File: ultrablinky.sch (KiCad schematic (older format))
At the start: 124 parts, among them J1 DNP, J2 SJ1-3523N, J3 SJ1-3523N, J4 Barrel_Jack_5.5x2.5, J5 DNP, J6 DNP, J7 Terminal5, J8 SJ1-3523N, Q1 DMP6180SK3Q-13, Q2 DMP6180SK3Q-13, Q4 MMBT3906, Q5 MMBT3904, Q6 MMBT3904, Q7 IRFZ44ZPBF, Q8 MMBT3904, SW1 SW_SPDT, SW2 PEC11R-4215F-S0024, SW3 SW_Push, U1 SGTL5000, U10 74VHC1G09, U2 TPS73618DBV, U3 Teensy4.0, U4 4N25, U5 LM2574HVM-5, U6 MC34071ADR2G, U7 DNP, U8 MCP4706A1T-E/CH, U9 VXO7803-500

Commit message: Changed film caps to electrolytic
The film caps in the audio path were changed to electrolytic in order to
bring down the cost and have better availability
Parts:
- C15, C23, C28: Source Mouser 80-C0805C101J1G -> Mouser 80-C0805C101J1G
- C2, C3, C5, C6: footprint 0_my_footprints:RSBCC4220Z310K_film_cap -> Capacitor_SMD:CP_Elec_4x5.7; symbol Device:C -> Device:CP; Source Mouser 80-RSBCC4220Z310K -> Mouser 710-865080140002
- C4: footprint 0_my_footprints:RSBCC4220Z310K_film_cap -> Capacitor_SMD:CP_Elec_4x5.7; symbol Device:C -> Device:CP; Source Mouser 80-RSBCC4220Z310K -> (none)
- R1: Source Mouser 603-RC0805JR-132K2L -> (none)
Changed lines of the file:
@@
 F 2 "Capacitor_SMD:C_0805_2012Metric" H 1738 8450 50  0001 C CNN
 F 3 "~" H 1700 8600 50  0001 C CNN
-F 4 "Mouser 80-C0805C101J1G " H 1700 8600 50  0001 C CNN "Source"
+F 4 "Mouser 80-C0805C101J1G" H 1700 8600 50  0001 C CNN "Source"
 	1    1700 8600
 	1    0    0    -1
@@
 F 2 "Capacitor_SMD:C_0805_2012Metric" H 13838 2000 50  0001 C CNN
 F 3 "~" H 13800 2150 50  0001 C CNN
-F 4 "Mouser 80-C0805C101J1G " H 13800 2150 50  0001 C CNN "Source"
+F 4 "Mouser 80-C0805C101J1G" H 13800 2150 50  0001 C CNN "Source"
 	1    13800 2150
 	1    0    0    -1
@@
 F 2 "Resistor_SMD:R_0805_2012Metric" V 11530 6650 50  0001 C CNN
 F 3 "~" H 11600 6650 50  0001 C CNN
-F 4 "Mouser 603-RC0805JR-132K2L" H 11600 6650 50  0001 C CNN "Source"
+F 4 "~" H 11600 6650 50  0001 C CNN "Source"
 	1    11600 6650
 	0    -1   1    0
@@
 $EndComp
 $Comp
-L Device:C C3
+L Device:CP C3
 U 1 1 61893B69
 P 11900 6050
-F 0 "C3" V 11850 6200 50  0000 C CNN
+F 0 "C3" V 11850 6250 50  0000 C CNN
 F 1 "2.2uF" V 11850 5900 50  0000 C CNN
-F 2 "0_my_footprints:RSBCC4220Z310K_film_cap" H 11938 5900 50  0001 C CNN
+F 2 "Capacitor_SMD:CP_Elec_4x5.7" H 11938 5900 50  0001 C CNN
 F 3 "~" H 11900 6050 50  0001 C CNN
-F 4 "Mouser 80-RSBCC4220Z310K" H 11900 6050 50  0001 C CNN "Source"
+F 4 "Mouser 710-865080140002" H 11900 6050 50  0001 C CNN "Source"
 	1    11900 6050
 	0    1    1    0
 $EndComp
 $Comp
-L Device:C C2
+L Device:CP C2
 U 1 1 61899EFD
 P 11900 6250
-F 0 "C2" V 11850 6400 50  0000 C CNN
+F 0 "C2" V 11850 6450 50  0000 C CNN
 F 1 "2.2uF" V 11850 6100 50  0000 C CNN
-F 2 "0_my_footprints:RSBCC4220Z310K_film_cap" H 11938 6100 50  0001 C CNN
+F 2 "Capacitor_SMD:CP_Elec_4x5.7" H 11938 6100 50  0001 C CNN
 F 3 "~" H 11900 6250 50  0001 C CNN
-F 4 "Mouser 80-RSBCC4220Z310K" H 11900 6250 50  0001 C CNN "Source"
+F 4 "Mouser 710-865080140002" H 11900 6250 50  0001 C CNN "Source"
 	1    11900 6250
 	0    1    1    0
 $EndComp
 $Comp
-L Device:C C4
+L Device:CP C4
 U 1 1 6189A492
 P 11900 6500
-F 0 "C4" V 11850 6650 50  0000 C CNN
+F 0 "C4" V 11850 6700 50  0000 C CNN
 F 1 "DNP" V 11850 6350 50  0000 C CNN
-F 2 "0_my_footprints:RSBCC4220Z310K_film_cap" H 11938 6350 50  0001 C CNN
+F 2 "Capacitor_SMD:CP_Elec_4x5.7" H 11938 6350 50  0001 C CNN
 F 3 "~" H 11900 6500 50  0001 C CNN
-F 4 "Mouser 80-RSBCC4220Z310K" H 11900 6500 50  0001 C CNN "Source"
+F 4 "~" H 11900 6500 50  0001 C CNN "Source"
 	1    11900 6500
 	0    1    1    0
 $EndComp
 $Comp
-L Device:C C6
+L Device:CP C6
 U 1 1 6189AB69
 P 14700 6400
-F 0 "C6" V 14450 6400 50  0000 C CNN
-F 1 "2.2uF" V 14550 6400 50  0000 C CNN
-F 2 "0_my_footprints:RSBCC4220Z310K_film_cap" H 14738 6250 50  0001 C CNN
+F 0 "C6" V 14950 6400 50  0000 C CNN
+F 1 "2.2uF" V 14850 6400 50  0000 C CNN
+F 2 "Capacitor_SMD:CP_Elec_4x5.7" H 14738 6250 50  0001 C CNN
 F 3 "~" H 14700 6400 50  0001 C CNN
-F 4 "Mouser 80-RSBCC4220Z310K" H 14700 6400 50  0001 C CNN "Source"
+F 4 "Mouser 710-865080140002" H 14700 6400 50  0001 C CNN "Source"
 	1    14700 6400
-	0    1    1    0
-$EndComp
-$Comp
-L Device:C C5
+	0    -1   -1   0
+$EndComp
+$Comp
+L Device:CP C5
 U 1 1 618A111E
 P 14700 6600
-F 0 "C5" V 14950 6600 50  0000 C CNN
-F 1 "2.2uF" V 14850 6600 50  0000 C CNN
-F 2 "0_my_footprints:RSBCC4220Z310K_film_cap" H 14738 6450 50  0001 C CNN
+F 0 "C5" V 14550 6600 50  0000 C CNN
+F 1 "2.2uF" V 14450 6600 50  0000 C CNN
+F 2 "Capacitor_SMD:CP_Elec_4x5.7" H 14738 6450 50  0001 C CNN
 F 3 "~" H 14700 6600 50  0001 C CNN
-F 4 "Mouser 80-RSBCC4220Z310K" H 14700 6600 50  0001 C CNN "Source"
+F 4 "Mouser 710-865080140002" H 14700 6600 50  0001 C CNN "Source"
 	1    14700 6600
-	0    1    1    0
+	0    -1   -1   0
 $EndComp
 $Comp
@@
 F 2 "Capacitor_SMD:C_0805_2012Metric" H 13588 2000 50  0001 C CNN
 F 3 "~" H 13550 2150 50  0001 C CNN
-F 4 "Mouser 80-C0805C101J1G " H 13550 2150 50  0001 C CNN "Source"
+F 4 "Mouser 80-C0805C101J1G" H 13550 2150 50  0001 C CNN "Source"
 	1    13550 2150
 	1    0    0    -1
@@
 L Graphic:Logo_Open_Hardware_Small #LOGO1
 U 1 1 60735E73
-P 8700 9600
-F 0 "#LOGO1" H 8700 9875 50  0001 C CNN
-F 1 "Logo_Open_Hardware_Small" H 8700 9375 50  0001 C CNN
-F 2 "Symbol:OSHW-Logo2_7.3x6mm_SilkScreen" H 8700 9600 50  0001 C CNN
-F 3 "~" H 8700 9600 50  0001 C CNN
-	1    8700 9600
-	1    0    0    -1
-$EndComp
+P 8600 9950
+F 0 "#LOGO1" H 8600 10225 50  0001 C CNN
+F 1 "Logo_Open_Hardware_Small" H 8600 9725 50  0001 C CNN
+F 2 "Symbol:OSHW-Logo2_7.3x6mm_SilkScreen" H 8600 9950 50  0001 C CNN
+F 3 "~" H 8600 9950 50  0001 C CNN
+	1    8600 9950
+	1    0    0    -1
+$EndComp

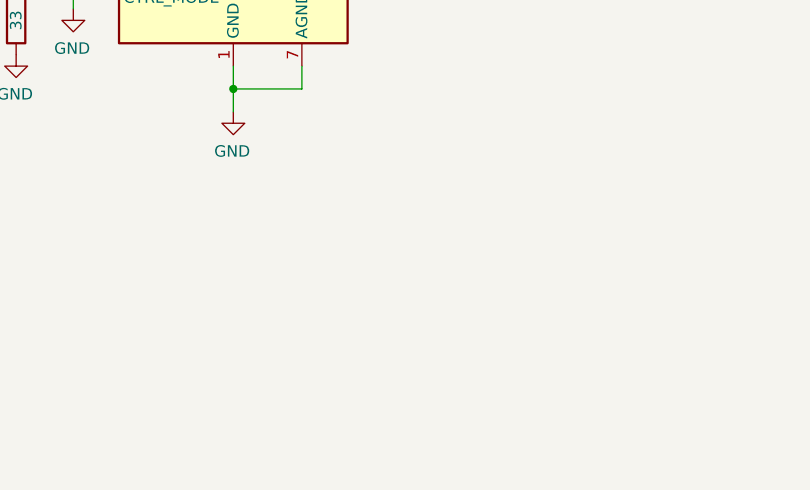
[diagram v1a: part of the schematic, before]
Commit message: Updated PCB with schematic changes
The rev B PCB now has the I2S SDIN and I2S SDOUT pins corrected. The
power supply has been changed to 48V. The PWM logic has been inverted.
The bus capacitance has been increased to 3300uF. The capacitors in the
audio path have been changed from film caps to electrolytic. The
Ultrablinky logo has been added.
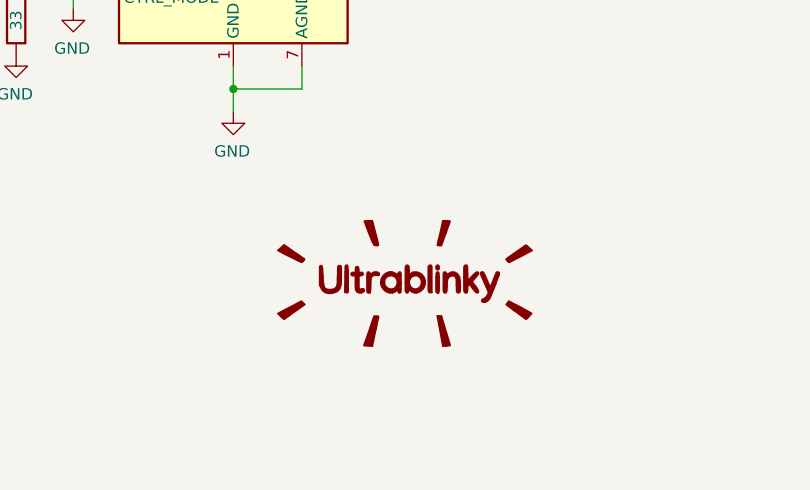
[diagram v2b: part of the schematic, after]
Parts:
- added LOGO1: Logo_Open_Hardware_Small, Symbol:OSHW-Logo2_9.8x8mm_SilkScreen, symbol Graphic:Logo_Open_Hardware_Small
- added LOGO2: Ultrablinky_logo, 0_project_footprints:logo_ultrablinky, symbol project_symbol_library:Ultrablinky_logo
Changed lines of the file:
@@
 	-1   0    0    -1
-$EndComp
-$Comp
-L Audio:SGTL5000XNAA3 U?
-U 1 1 614B24E2
-P 13550 7300
-AR Path="/60675ACD/614B24E2" Ref="U?"  Part="1"
-AR Path="/614B24E2" Ref="U1"  Part="1"
-F 0 "U1" H 14150 6450 50  0000 C CNN
-F 1 "SGTL5000" H 14400 6350 50  0000 C CNN
-F 2 "Package_DFN_QFN:QFN-32-1EP_5x5mm_P0.5mm_EP3.6x3.6mm" H 13550 7300 50  0001 C CNN
-F 3 "http://www.nxp.com/docs/en/data-sheet/SGTL5000.pdf" H 13550 7300 50  0001 C CNN
-F 4 "Mouser 841-SGTL5000XNAA3R2" H 13550 7300 50  0001 C CNN "Source"
-	1    13550 7300
-	1    0    0    -1
 $EndComp
 Wire Wire Line
@@
 NoConn ~ 14150 7000
 NoConn ~ 14150 7100
-NoConn ~ 14150 7200
 $Comp
 L Device:C C?
@@
 Connection ~ 1550 8800
 $Comp
-L Graphic:Logo_Open_Hardware_Small #LOGO1
+L Graphic:Logo_Open_Hardware_Small LOGO1
 U 1 1 60735E73
 P 8600 9950
-F 0 "#LOGO1" H 8600 10225 50  0001 C CNN
+F 0 "LOGO1" H 8600 10225 50  0001 C CNN
 F 1 "Logo_Open_Hardware_Small" H 8600 9725 50  0001 C CNN
-F 2 "Symbol:OSHW-Logo2_7.3x6mm_SilkScreen" H 8600 9950 50  0001 C CNN
+F 2 "Symbol:OSHW-Logo2_9.8x8mm_SilkScreen" H 8600 9950 50  0001 C CNN
 F 3 "~" H 8600 9950 50  0001 C CNN
 	1    8600 9950
@@
 Wire Wire Line
 	4550 8500 4800 8500
+NoConn ~ 14150 7200
+$Comp
+L Audio:SGTL5000XNAA3 U?
+U 1 1 614B24E2
+P 13550 7300
+AR Path="/60675ACD/614B24E2" Ref="U?"  Part="1"
+AR Path="/614B24E2" Ref="U1"  Part="1"
+F 0 "U1" H 14150 6450 50  0000 C CNN
+F 1 "SGTL5000" H 14400 6350 50  0000 C CNN
+F 2 "Package_DFN_QFN:QFN-32-1EP_5x5mm_P0.5mm_EP3.6x3.6mm" H 13550 7300 50  0001 C CNN
+F 3 "http://www.nxp.com/docs/en/data-sheet/SGTL5000.pdf" H 13550 7300 50  0001 C CNN
+F 4 "Mouser 841-SGTL5000XNAA3R2" H 13550 7300 50  0001 C CNN "Source"
+	1    13550 7300
+	1    0    0    -1
+$EndComp
+$Comp
+L project_symbol_library:Ultrablinky_logo LOGO2
+U 1 1 61166262
+P 14300 9550
+F 0 "LOGO2" H 14300 9306 60  0001 C CNN
+F 1 "Ultrablinky_logo" H 14300 9794 60  0001 C CNN
+F 2 "0_project_footprints:logo_ultrablinky" H 14300 9550 50  0001 C CNN
+F 3 "" H 14300 9550 50  0001 C CNN
+	1    14300 9550
+	1    0    0    -1
+$EndComp
 $EndSCHEMATC

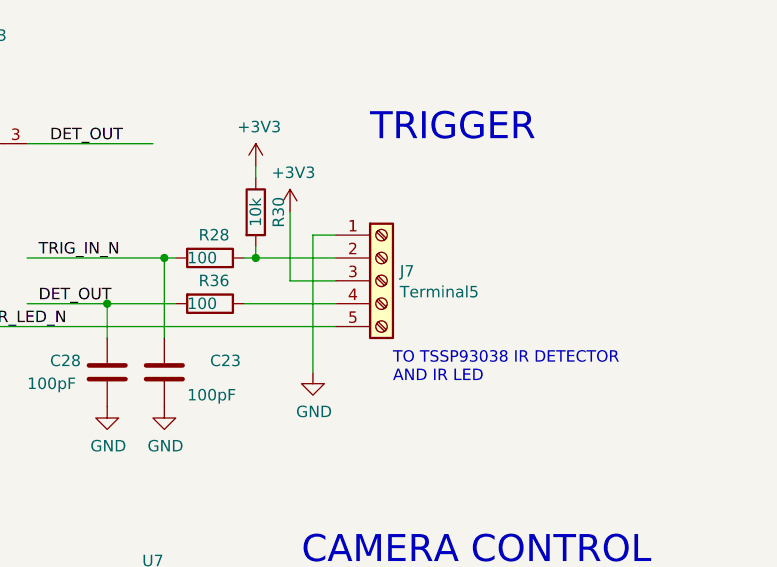
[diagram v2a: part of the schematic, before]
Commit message: Corrected 4N25 footprints
Previously the 4N25 footprints were too narrow for the pins.
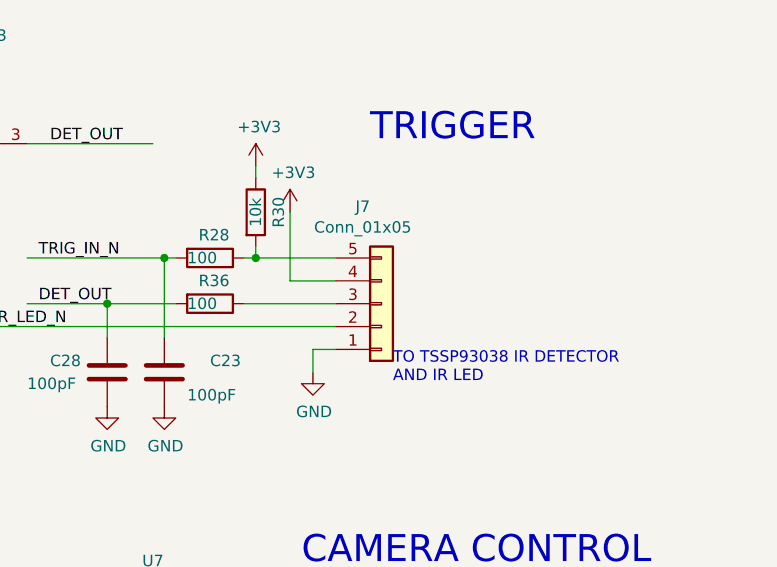
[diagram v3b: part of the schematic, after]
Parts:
- removed J7: Terminal5, 0_my_footprints:TerminalBlock_Molex_39532-1005,5-5.08_1x05_P5.08mm_Horizontal_Pluggable, symbol Connector:Screw_Terminal_01x05
- added J7: Conn_01x05, 0_my_footprints:Molex_Mini-Fit_Jr_39-30-3055_1x05_P4.20mm_Horizontal, symbol Connector_Generic:Conn_01x05
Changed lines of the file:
@@
 	1    0    0    -1
 $EndComp
-$Comp
-L Connector:Screw_Terminal_01x05 J7
-U 1 1 607E6AEB
-P 14750 1750
-F 0 "J7" H 14830 1792 50  0000 L CNN
-F 1 "Terminal5" H 14830 1701 50  0000 L CNN
-F 2 "0_my_footprints:TerminalBlock_Molex_39532-1005,5-5.08_1x05_P5.08mm_Horizontal_Pluggable" H 14750 1750 50  0001 C CNN
-F 3 "~" H 14750 1750 50  0001 C CNN
-F 4 "Mouser 538-39530-0005, Mouser 538-39532-1005" H 14750 1750 50  0001 C CNN "Source"
-	1    14750 1750
-	1    0    0    -1
-$EndComp
-Wire Wire Line
-	14550 1550 14450 1550
-Wire Wire Line
-	14450 1550 14450 2150
+Wire Wire Line
+	14550 2050 14450 2050
+Wire Wire Line
+	14450 2050 14450 2150
 $Comp
 L power:GND #PWR0137
@@
 	1    0    0    -1
 $EndComp
+$Comp
+L Connector_Generic:Conn_01x05 J7
+U 1 1 612E9888
+P 14750 1850
+F 0 "J7" H 14668 1425 50  0000 C CNN
+F 1 "Conn_01x05" H 14668 1516 50  0000 C CNN
+F 2 "0_my_footprints:Molex_Mini-Fit_Jr_39-30-3055_1x05_P4.20mm_Horizontal" H 14750 1850 50  0001 C CNN
+F 3 "~" H 14750 1850 50  0001 C CNN
+	1    14750 1850
+	1    0    0    1
+$EndComp
 $EndSCHEMATC

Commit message: Added two additional bypass caps
The voltage regulator for the op amp and the 74VHC1G09 did not have
bypass caps previously
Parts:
- added C27, C33: 10nF, Capacitor_SMD:C_0805_2012Metric, symbol Device:C
- C12: footprint Resistor_SMD:R_0805_2012Metric -> Capacitor_SMD:C_0805_2012Metric
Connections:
- wire segments 383 -> 395
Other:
- note added: "TO TSSP93038\nIR DETECTOR\nAND IR LED"
- note removed: "TO TSSP93038 IR DETECTOR\nAND IR LED"
- moved on the sheet: C17, C19, C20, C23, C24, C26, C28, C29, C30, D3, D4, DISP1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

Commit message: Eliminated 5v-3.3v regulator
The Teensy 4.0 has a 3.3V pin that can supply up to 250mA, so that is
now the source for 3.3V.
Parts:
- removed C31: 10uF, Capacitor_SMD:C_1206_3216Metric, symbol Device:C
- removed C32: 22uF, Capacitor_SMD:C_1210_3225Metric, symbol Device:C
- removed J5: DNP, Connector_PinHeader_2.54mm:PinHeader_1x03_P2.54mm_Vertical, symbol Connector_Generic:Conn_01x03
- removed U9: VXO7803-500, 0_my_footprints:VXO780x-500, symbol 0_my_symbols:VXO7803-500
- renumbered C17 to C16, C19 to C17, C20 to C18, C33 to C19, C21 to C20, C22 to C21, C18 to C22, C27 to C23, C23 to C24, C24 to C25, C25 to C26, C26 to C27, C4 to C3, C16 to C31, C3 to C4, D6 to D2, D2 to D3, D3 to D4, D7 to D5, D4 to D6, D5 to D7, J6 to J5, J8 to J6, LOGO2 to LOGO1, LOGO1 to LOGO2, Q8 to Q3, R9 to R10, R14 to R12, R12 to R13, R13 to R14, R45 to R15, R15 to R16, R16 to R17, R17 to R20, R20 to R21, R21 to R22, R22 to R23, R23 to R24, R24 to R25, R25 to R26, R32 to R27, R26 to R28, R27 to R29, R44 to R30, R28 to R31, R35 to R32, R29 to R33, R30 to R34, R31 to R35, R33 to R36, R34 to R37, R36 to R38, R37 to R39, R38 to R40, R39 to R41, R40 to R42, R41 to R43, R42 to R44, R43 to R45, R10 to R9, U10 to U7, U7 to U8, U8 to U9
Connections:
- wire segments 395 -> 385
- no-connect marks 24 -> 25
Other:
- note added: "5.0mA"

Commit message: General cleanup and generate Gerbers
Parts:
- U7: footprint Package_TO_SOT_SMD:SOT-353_SC-70-5 -> Package_TO_SOT_SMD:SOT-353_SC-70-5_Handsoldering
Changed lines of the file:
@@
 F 0 "U7" H 2800 7650 50  0000 C CNN
 F 1 "74VHC1G09" H 2950 7550 50  0000 C CNN
-F 2 "Package_TO_SOT_SMD:SOT-353_SC-70-5" H 2650 7400 50  0001 C CNN
+F 2 "Package_TO_SOT_SMD:SOT-353_SC-70-5_Handsoldering" H 2650 7400 50  0001 C CNN
 F 3 "https://www.onsemi.com/pdf/datasheet/mc74vhc1g09-d.pdf" H 2650 7400 50  0001 C CNN
 F 4 "Mouser 863-MC74VHC1G09DFT2G" H 2650 7400 50  0001 C CNN "Source"

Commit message: Changed 22uF cap to 10uF to reduce BOM cost
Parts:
- C1: Source Mouser 810-CGA5L1X7R1H106K1 -> (none)
- C10, C13, C16, C29: Source Mouser 187-CL31B106KOHNNWE -> Mouser 187-CL31A106MBHNNNE
- C11, C14, C22, C7, C8, C9: Source Mouser 80-C0805C104K5R -> Mouser 710-885012207128
- C12, C17, C18, C19, C23, C25, C27, C30: Source Mouser 80-C0805C103K1R -> Mouser 581-08051C103K
- C21: value 22uF -> 10uF; footprint Capacitor_SMD:C_1210_3225Metric -> Capacitor_SMD:C_1206_3216Metric; Source Mouser 187-CL32A226MOJNNNE -> Mouser 187-CL31A106MBHNNNE
- DISP1: Source PJRC DISPLAY_ILI9341_TOUCH, Mouser 200-SLW11401TS, Mouser 5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 -> PJRC DISPLAY_ILI9341_TOUCH, Mouser 200-SSW11401TS, Mouser 5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
- J7: Source (none) -> Mouser 538-39-30-3055, Mouser 538-03-04-4052, Mouser 538-39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
- U3: Source PJRC TEENSY40, Mouser 649-68000-136, Mouser 200-SLW11401TS -> PJRC TEENSY40, Mouser 649-68000-136, Mouser 200-SSW11401TS
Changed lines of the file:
@@
 F 2 "Capacitor_SMD:C_0805_2012Metric" H 2488 5750 50  0001 C CNN
 F 3 "~" H 2450 5900 50  0001 C CNN
-F 4 "Mouser 80-C0805C103K1R" H 2450 5900 50  0001 C CNN "Source"
+F 4 "Mouser 581-08051C103K" H 2450 5900 50  0001 C CNN "Source"
 	1    2450 5900
 	0    1    1    0
@@
 P 3900 6250
 F 0 "C21" V 3750 6350 50  0000 L CNN
-F 1 "22uF" V 3850 6350 50  0000 L CNN
-F 2 "Capacitor_SMD:C_1210_3225Metric" H 3938 6100 50  0001 C CNN
+F 1 "10uF" V 3850 6350 50  0000 L CNN
+F 2 "Capacitor_SMD:C_1206_3216Metric" H 3938 6100 50  0001 C CNN
 F 3 "~" H 3900 6250 50  0001 C CNN
-F 4 "Mouser 187-CL32A226MOJNNNE" H 3900 6250 50  0001 C CNN "Source"
+F 4 "Mouser 187-CL31A106MBHNNNE" H 3900 6250 50  0001 C CNN "Source"
 	1    3900 6250
 	0    1    1    0
@@
 F 2 "Capacitor_SMD:C_0805_2012Metric" H 8538 4100 50  0001 C CNN
 F 3 "~" H 8500 4250 50  0001 C CNN
-F 4 "Mouser 80-C0805C103K1R" H 8500 4250 50  0001 C CNN "Source"
+F 4 "Mouser 581-08051C103K" H 8500 4250 50  0001 C CNN "Source"
 	1    8500 4250
 	1    0    0    -1
@@
 F 2 "Capacitor_SMD:C_0805_2012Metric" H 8288 4100 50  0001 C CNN
 F 3 "~" H 8250 4250 50  0001 C CNN
-F 4 "Mouser 80-C0805C103K1R" H 8250 4250 50  0001 C CNN "Source"
+F 4 "Mouser 581-08051C103K" H 8250 4250 50  0001 C CNN "Source"
 	1    8250 4250
 	1    0    0    -1
@@
 F 2 "Capacitor_SMD:C_1206_3216Metric" H 13238 5300 50  0001 C CNN
 F 3 "~" H 13200 5450 50  0001 C CNN
-F 4 "Mouser 187-CL31B106KOHNNWE" H 13200 5450 50  0001 C CNN "Source"
+F 4 "Mouser 187-CL31A106MBHNNNE" H 13200 5450 50  0001 C CNN "Source"
 	1    13200 5450
 	1    0    0    -1
@@
 F 2 "Resistor_SMD:R_0805_2012Metric" H 12938 5300 50  0001 C CNN
 F 3 "~" H 12900 5450 50  0001 C CNN
-F 4 "Mouser 80-C0805C104K5R" H 12900 5450 50  0001 C CNN "Source"
+F 4 "Mouser 710-885012207128" H 12900 5450 50  0001 C CNN "Source"
 	1    12900 5450
 	1    0    0    -1
@@
 F 2 "Resistor_SMD:R_0805_2012Metric" H 13838 5150 50  0001 C CNN
 F 3 "~" H 13800 5300 50  0001 C CNN
-F 4 "Mouser 80-C0805C104K5R" H 13800 5300 50  0001 C CNN "Source"
+F 4 "Mouser 710-885012207128" H 13800 5300 50  0001 C CNN "Source"
 	1    13800 5300
 	1    0    0    -1
@@
 F 2 "Capacitor_SMD:C_1206_3216Metric" H 14638 5350 50  0001 C CNN
 F 3 "~" H 14600 5500 50  0001 C CNN
-F 4 "Mouser 187-CL31B106KOHNNWE" H 14600 5500 50  0001 C CNN "Source"
+F 4 "Mouser 187-CL31A106MBHNNNE" H 14600 5500 50  0001 C CNN "Source"
 	1    14600 5500
 	1    0    0    -1
@@
 F 2 "Resistor_SMD:R_0805_2012Metric" H 14338 5350 50  0001 C CNN
 F 3 "~" H 14300 5500 50  0001 C CNN
-F 4 "Mouser 80-C0805C104K5R" H 14300 5500 50  0001 C CNN "Source"
+F 4 "Mouser 710-885012207128" H 14300 5500 50  0001 C CNN "Source"
 	1    14300 5500
 	1    0    0    -1
@@
 F 2 "Resistor_SMD:R_0805_2012Metric" H 12538 5900 50  0001 C CNN
 F 3 "~" H 12500 6050 50  0001 C CNN
-F 4 "Mouser 80-C0805C104K5R" H 12500 6050 50  0001 C CNN "Source"
+F 4 "Mouser 710-885012207128" H 12500 6050 50  0001 C CNN "Source"
 	1    12500 6050
 	1    0    0    -1
@@
 F 2 "Capacitor_SMD:C_1206_3216Metric" H 11838 6700 50  0001 C CNN
 F 3 "~" H 11800 6850 50  0001 C CNN
-F 4 "Mouser 810-CGA5L1X7R1H106K1" H 11800 6850 50  0001 C CNN "Source"
+F 4 "~" H 11800 6850 50  0001 C CNN "Source"
 	1    11800 6850
 	-1   0    0    -1
@@
 F 2 "Resistor_SMD:R_0805_2012Metric" H 11238 5200 50  0001 C CNN
 F 3 "~" H 11200 5350 50  0001 C CNN
-F 4 "Mouser 80-C0805C104K5R" H 11200 5350 50  0001 C CNN "Source"
+F 4 "Mouser 710-885012207128" H 11200 5350 50  0001 C CNN "Source"
 	1    11200 5350
 	1    0    0    -1
@@
 F 2 "Capacitor_SMD:C_0805_2012Metric" H 12438 5350 50  0001 C CNN
 F 3 "~" H 12400 5500 50  0001 C CNN
-F 4 "Mouser 80-C0805C103K1R" H 12400 5500 50  0001 C CNN "Source"
+F 4 "Mouser 581-08051C103K" H 12400 5500 50  0001 C CNN "Source"
 	1    12400 5500
 	1    0    0    -1
@@
 F 2 "0_my_footprints:Teensy40" H 4300 2600 50  0001 C CNN
 F 3 "https://www.pjrc.com/store/teensy40.html" H 4300 2600 50  0001 C CNN
-F 4 "PJRC TEENSY40, Mouser 649-68000-136, Mouser 200-SLW11401TS" H 4700 2400 50  0001 C CNN "Source"
+F 4 "PJRC TEENSY40, Mouser 649-68000-136, Mouser 200-SSW11401TS" H 4700 2400 50  0001 C CNN "Source"
 	1    4700 2400
 	1    0    0    -1
@@
 F 2 "Capacitor_SMD:C_0805_2012Metric" H 9138 5300 50  0001 C CNN
 F 3 "~" H 9100 5450 50  0001 C CNN
-F 4 "Mouser 80-C0805C103K1R" H 9100 5450 50  0001 C CNN "Source"
+F 4 "Mouser 581-08051C103K" H 9100 5450 50  0001 C CNN "Source"
 	1    9100 5450
 	1    0    0    -1
@@
 F 2 "Capacitor_SMD:C_0805_2012Metric" H 10738 4050 50  0001 C CNN
 F 3 "~" H 10700 4200 50  0001 C CNN
-F 4 "Mouser 80-C0805C103K1R" H 10700 4200 50  0001 C CNN "Source"
+F 4 "Mouser 581-08051C103K" H 10700 4200 50  0001 C CNN "Source"
 	1    10700 4200
 	-1   0    0    -1
@@
 F 2 "0_my_footprints:DISPLAY_ILI9341_TOUCH" H 10150 800 50  0001 C CNN
 F 3 "" H 10050 850 50  0001 C CNN
-F 4 "PJRC DISPLAY_ILI9341_TOUCH, Mouser 200-SLW11401TS, Mouser 534-25511  x4, Mouser 144-50M030050P006 x 8" H 10150 2100 50  0001 C CNN "Source"
+F 4 "PJRC DISPLAY_ILI9341_TOUCH, Mouser 200-SSW11401TS, Mouser 534-25511  x4, Mouser 144-50M030050P006 x 8" H 10150 2100 50  0001 C CNN "Source"
 	1    10150 2100
 	1    0    0    -1
@@
 F 2 "Capacitor_SMD:C_1206_3216Metric" H 9588 950 50  0001 C CNN
 F 3 "~" H 9550 1100 50  0001 C CNN
-F 4 "Mouser 187-CL31B106KOHNNWE" H 9550 1100 50  0001 C CNN "Source"
+F 4 "Mouser 187-CL31A106MBHNNNE" H 9550 1100 50  0001 C CNN "Source"
 	1    9550 1100
 	1    0    0    -1
@@
 F 2 "Capacitor_SMD:C_1206_3216Metric" H 6638 2950 50  0001 C CNN
 F 3 "~" H 6600 3100 50  0001 C CNN
-F 4 "Mouser 187-CL31B106KOHNNWE" H 6600 3100 50  0001 C CNN "Source"
+F 4 "Mouser 187-CL31A106MBHNNNE" H 6600 3100 50  0001 C CNN "Source"
 	1    6600 3100
 	1    0    0    -1
@@
 F 2 "Resistor_SMD:R_0805_2012Metric" H 4838 8600 50  0001 C CNN
 F 3 "~" H 4800 8750 50  0001 C CNN
-F 4 "Mouser 80-C0805C104K5R" H 4800 8750 50  0001 C CNN "Source"
+F 4 "Mouser 710-885012207128" H 4800 8750 50  0001 C CNN "Source"
 	1    4800 8750
 	1    0    0    -1
@@
 F 2 "0_my_footprints:Molex_Mini-Fit_Jr_39-30-3055_1x05_P4.20mm_Horizontal" H 15300 2050 50  0001 C CNN
 F 3 "~" H 15300 2050 50  0001 C CNN
+F 4 "Mouser 538-39-30-3055, Mouser 538-03-04-4052, Mouser 538-39-00-0060 x 5" H 15300 2050 50  0001 C CNN "Source"
 	1    15300 2050
 	1    0    0    1
@@
 F 2 "Capacitor_SMD:C_0805_2012Metric" H 2338 6950 50  0001 C CNN
 F 3 "~" H 2300 7100 50  0001 C CNN
-F 4 "Mouser 80-C0805C103K1R" H 2300 7100 50  0001 C CNN "Source"
+F 4 "Mouser 581-08051C103K" H 2300 7100 50  0001 C CNN "Source"
 	1    2300 7100
 	0    1    1    0
@@
 F 2 "Capacitor_SMD:C_0805_2012Metric" H 3938 4800 50  0001 C CNN
 F 3 "~" H 3900 4950 50  0001 C CNN
-F 4 "Mouser 80-C0805C103K1R" H 3900 4950 50  0001 C CNN "Source"
+F 4 "Mouser 581-08051C103K" H 3900 4950 50  0001 C CNN "Source"
 	1    3900 4950
 	0    1    1    0
